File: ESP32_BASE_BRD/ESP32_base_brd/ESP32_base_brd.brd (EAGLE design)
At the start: 100 x 80 mm, 22 parts, among them IC3 TPS63802DLAR, U1 ESP-WROOM-32

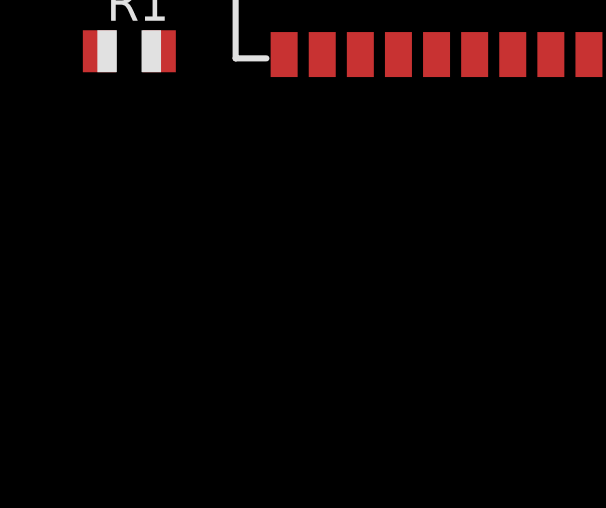
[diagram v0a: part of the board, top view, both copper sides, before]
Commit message: add transistor to load program without push buttons and flip boot led
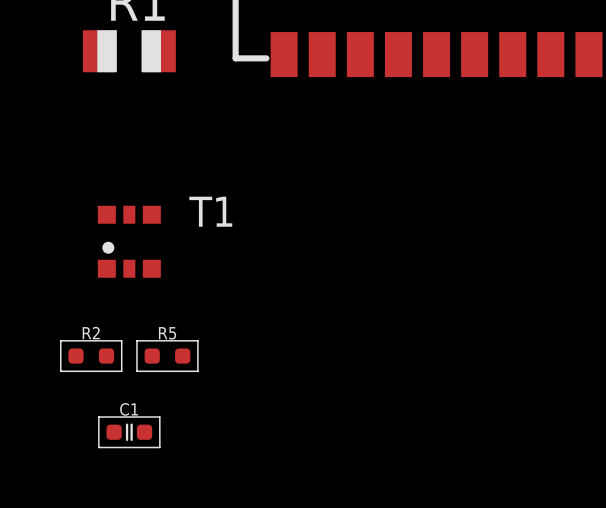
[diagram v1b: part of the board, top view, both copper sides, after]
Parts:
- added C1: 100nF 50V, vb_C_EC:0402
- added R2, R5: 10k, vb_R_EC:0402
- added T1: BC846S, BC846S:SOT363
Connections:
- new net DTR: R2.2, T1.1
- new net N$1: R2.1, T1.5
- new net N$2: R5.1, T1.2
- new net RTS: R5.2, T1.4
- net 3V3: no longer D1.+
- net BOOT_LED: now also D1.+; no longer R3.1
- net EN: now also C1.2, T1.3
- net GND: now also C1.1, R3.1
- net IO0: now also T1.6
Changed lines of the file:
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@@
 <attribute name="VALUE" x="-38.24" y="12.7" size="0.8128" layer="27" rot="R90" align="center"/>
+</element>
+<element name="T1" library="BC846S" package="SOT363" value="BC846S" x="-45.72" y="-2.54" smashed="yes">
+<attribute name="AVAILABILITY" value="In Stock" x="-45.72" y="-2.54" size="1.778" layer="27" display="off"/>
+<attribute name="DESCRIPTION" value=" Bipolar (BJT) Transistor Array 2 NPN (Dual) 65V 100mA 100MHz 300mW Surface Mount 6-TSSOP " x="-45.72" y="-2.54" size="1.778" layer="27" display="off"/>
+<attribute name="MF" value="NXP Semiconductors" x="-45.72" y="-2.54" size="1.778" layer="27" display="off"/>
+<attribute name="MP" value="BC846S" x="-45.72" y="-2.54" size="1.778" layer="27" display="off"/>
+<attribute name="NAME" x="-43.71741875" y="-2.03935625" size="1.001290625" layer="25"/>
+<attribute name="PACKAGE" value="SOT-363 NXP Semiconductors" x="-45.72" y="-2.54" size="1.778" layer="27" display="off"/>
+<attribute name="PRICE" value="None" x="-45.72" y="-2.54" size="1.778" layer="27" display="off"/>
+<attribute name="PURCHASE-URL" value="https://pricing.snapeda.com/search/part/BC846S/?ref=eda" x="-45.72" y="-2.54" size="1.778" layer="27" display="off"/>
+<attribute name="VALUE" x="-43.719909375" y="-3.54005" size="1.00005" layer="27"/>
+</element>
+<element name="R2" library="vb_R_EC" package="0402" value="10k" x="-46.99" y="-6.35" smashed="yes">
+<attribute name="NAME" x="-46.99" y="-5.588" size="0.4064" layer="25" align="center"/>
+<attribute name="VALUE" x="-46.99" y="-6.35" size="0.4064" layer="27" align="center"/>
+</element>
+<element name="R5" library="vb_R_EC" package="0402" value="10k" x="-44.45" y="-6.35" smashed="yes">
+<attribute name="NAME" x="-44.45" y="-5.588" size="0.4064" layer="25" align="center"/>
+<attribute name="VALUE" x="-44.45" y="-6.35" size="0.4064" layer="27" align="center"/>
+</element>
+<element name="C1" library="vb_C_EC" package="0402" value="100nF 50V" x="-45.72" y="-8.89" smashed="yes">
+<attribute name="MPN" value="GPC0402104" x="-45.72" y="-8.89" size="1.778" layer="27" display="off"/>
+<attribute name="NAME" x="-45.72" y="-8.128" size="0.4064" layer="25" align="center"/>
+<attribute name="VALUE" x="-45.72" y="-8.89" size="0.4064" layer="27" align="center"/>
 </element>
 </elements>
@@
 <contactref element="R10" pad="1"/>
 <contactref element="R26" pad="1"/>
-<wire x1="-38.95" y1="26.67" x2="-42.05" y2="18.415" width="0" layer="19" extent="1-1"/>
-<wire x1="-45.3" y1="26.67" x2="-38.95" y2="26.67" width="0" layer="19" extent="1-1"/>
-<wire x1="-40.64" y1="33.02" x2="-38.95" y2="26.67" width="0" layer="19" extent="1-1"/>
-<wire x1="-37.29" y1="33.02" x2="-40.64" y2="33.02" width="0" layer="19" extent="1-1"/>
-<wire x1="-41.148" y1="38.1" x2="-40.64" y2="33.02" width="0" layer="19" extent="1-1"/>
-<wire x1="-47.498" y1="38.1" x2="-41.148" y2="38.1" width="0" layer="19" extent="1-1"/>
-<wire x1="-27.57" y1="28.44" x2="-37.29" y2="33.02" width="0" layer="19" extent="1-1"/>
-<wire x1="-27.57" y1="27.94" x2="-27.57" y2="28.44" width="0" layer="19" extent="1-1"/>
-<wire x1="-26.12" y1="27.94" x2="-27.57" y2="27.94" width="0" layer="19" extent="1-1"/>
+<contactref element="C1" pad="1"/>
+<contactref element="R3" pad="1"/>
+<wire x1="-24.05" y1="3.7" x2="-46.228" y2="-8.89" width="0" layer="19" extent="1-1"/>
+<wire x1="-24.05" y1="21.7" x2="-24.05" y2="3.7" width="0" layer="19" extent="1-1"/>
+<wire x1="-26.12" y1="27.94" x2="-24.05" y2="21.7" width="0" layer="19" extent="1-1"/>
+<wire x1="-27.57" y1="27.94" x2="-26.12" y2="27.94" width="0" layer="19" extent="1-1"/>
+<wire x1="-27.57" y1="28.44" x2="-27.57" y2="27.94" width="0" layer="19" extent="1-1"/>
 <wire x1="-24.98" y1="34.29" x2="-27.57" y2="28.44" width="0" layer="19" extent="1-1"/>
 <wire x1="-18.63" y1="34.29" x2="-24.98" y2="34.29" width="0" layer="19" extent="1-1"/>
-<wire x1="-24.05" y1="21.7" x2="-26.12" y2="27.94" width="0" layer="19" extent="1-1"/>
 <wire x1="-24.638" y1="41.91" x2="-24.98" y2="34.29" width="0" layer="19" extent="1-1"/>
 <wire x1="-19.558" y1="41.91" x2="-24.638" y2="41.91" width="0" layer="19" extent="1-1"/>
-<wire x1="-24.05" y1="3.7" x2="-24.05" y2="21.7" width="0" layer="19" extent="1-1"/>
+<wire x1="-37.29" y1="33.02" x2="-27.57" y2="28.44" width="0" layer="19" extent="1-1"/>
+<wire x1="-40.64" y1="33.02" x2="-37.29" y2="33.02" width="0" layer="19" extent="1-1"/>
+<wire x1="-41.148" y1="38.1" x2="-40.64" y2="33.02" width="0" layer="19" extent="1-1"/>
+<wire x1="-44.958" y1="38.1" x2="-41.148" y2="38.1" width="0" layer="19" extent="1-1"/>
+<wire x1="-47.498" y1="38.1" x2="-44.958" y2="38.1" width="0" layer="19" extent="1-1"/>
+<wire x1="-38.95" y1="26.67" x2="-37.29" y2="33.02" width="0" layer="19" extent="1-1"/>
+<wire x1="-45.3" y1="26.67" x2="-38.95" y2="26.67" width="0" layer="19" extent="1-1"/>
+<wire x1="-42.05" y1="18.415" x2="-38.95" y2="26.67" width="0" layer="19" extent="1-1"/>
 </signal>
 <signal name="!CS_ESP">
@@
 <contactref element="R1" pad="2"/>
 <contactref element="D6" pad="+"/>
-<contactref element="D1" pad="+"/>
 <contactref element="R7" pad="2"/>
 <contactref element="D2" pad="+"/>
@@
 <wire x1="-23.28" y1="34.29" x2="-15.51" y2="27.94" width="0" layer="19" extent="1-1"/>
 <wire x1="-24.5925" y1="38.1" x2="-23.28" y2="34.29" width="0" layer="19" extent="1-1"/>
-<wire x1="-20.7825" y1="38.1" x2="-24.5925" y2="38.1" width="0" layer="19" extent="1-1"/>
 <wire x1="-28.4025" y1="38.1" x2="-24.5925" y2="38.1" width="0" layer="19" extent="1-1"/>
 <wire x1="-35.9292" y1="38.1" x2="-28.4025" y2="38.1" width="0" layer="19" extent="1-1"/>
@@
 <contactref element="R1" pad="1"/>
 <contactref element="U1" pad="3"/>
+<contactref element="T1" pad="3"/>
+<contactref element="C1" pad="2"/>
+<wire x1="-44.97" y1="-3.44" x2="-45.212" y2="-8.89" width="0" layer="19" extent="1-1"/>
+<wire x1="-46.72" y1="3.81" x2="-44.97" y2="-3.44" width="0" layer="19" extent="1-1"/>
 <wire x1="-26.59" y1="21.7" x2="-46.72" y2="3.81" width="0" layer="19" extent="1-1"/>
 </signal>
@@
 <signal name="BOOT_LED">
 <contactref element="U1" pad="16"/>
-<contactref element="R3" pad="1"/>
-<wire x1="-44.958" y1="38.1" x2="-42.05" y2="17.145" width="0" layer="19" extent="1-1"/>
+<contactref element="D1" pad="+"/>
+<wire x1="-20.7825" y1="38.1" x2="-42.05" y2="17.145" width="0" layer="19" extent="1-1"/>
 </signal>
 <signal name="N$7">
@@
 <signal name="IO0">
 <contactref element="U1" pad="25"/>
+<contactref element="T1" pad="6"/>
+<wire x1="-40.56" y1="3.7" x2="-46.47" y2="-1.64" width="0" layer="19" extent="1-1"/>
+</signal>
+<signal name="N$1">
+<contactref element="T1" pad="5"/>
+<contactref element="R2" pad="1"/>
+<wire x1="-45.72" y1="-1.64" x2="-47.498" y2="-6.35" width="0" layer="19" extent="1-1"/>
+</signal>
+<signal name="N$2">
+<contactref element="T1" pad="2"/>
+<contactref element="R5" pad="1"/>
+<wire x1="-44.958" y1="-6.35" x2="-45.72" y2="-3.44" width="0" layer="19" extent="1-1"/>
+</signal>
+<signal name="DTR">
+<contactref element="R2" pad="2"/>
+<contactref element="T1" pad="1"/>
+<wire x1="-46.47" y1="-3.44" x2="-46.482" y2="-6.35" width="0" layer="19" extent="1-1"/>
+</signal>
+<signal name="RTS">
+<contactref element="R5" pad="2"/>
+<contactref element="T1" pad="4"/>
+<wire x1="-44.97" y1="-1.64" x2="-43.942" y2="-6.35" width="0" layer="19" extent="1-1"/>
 </signal>
 </signals>
